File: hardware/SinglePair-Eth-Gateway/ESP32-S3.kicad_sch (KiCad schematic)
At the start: 16 parts, among them J201 Conn_01x06_Pin, J202 Conn_01x04, J203 USB_B_Micro, U201 WE-TVS-82400102

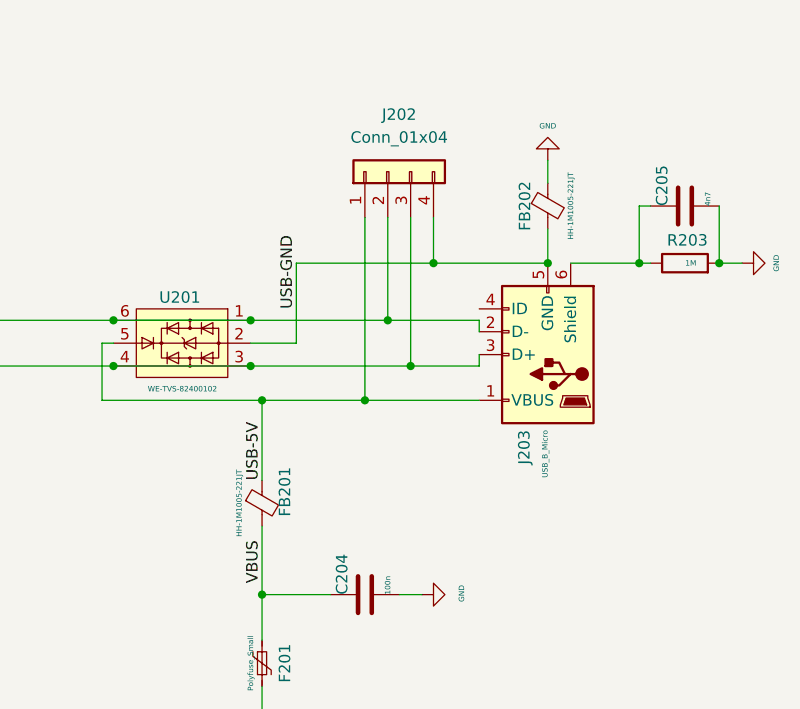
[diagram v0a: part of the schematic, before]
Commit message: Change position of values on the Fab layer
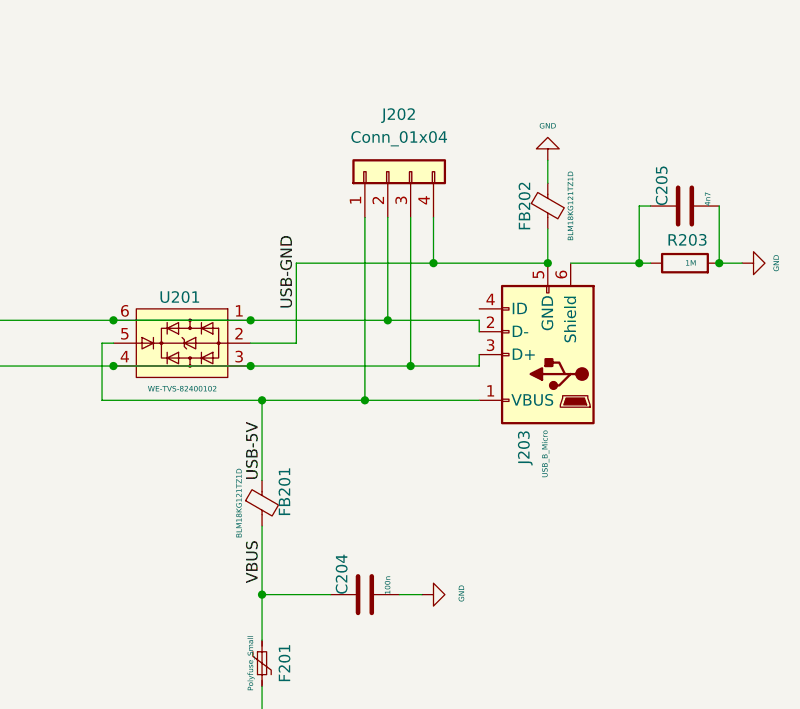
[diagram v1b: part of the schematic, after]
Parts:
- FB201, FB202: value HH-1M1005-221JT -> BLM18KG121TZ1D
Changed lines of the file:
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@@
       (effects (font (size 1.27 1.27)))
     )
-    (property "Value" "HH-1M1005-221JT" (at 264.16 181.61 90)
+    (property "Value" "BLM18KG121TZ1D" (at 264.16 181.61 90)
       (effects (font (size 0.6 0.6)))
     )
@@
       (effects (font (size 1.27 1.27)))
     )
-    (property "Value" "HH-1M1005-221JT" (at 300.99 148.59 90)
+    (property "Value" "BLM18KG121TZ1D" (at 300.99 148.59 90)
       (effects (font (size 0.6 0.6)))
     )
